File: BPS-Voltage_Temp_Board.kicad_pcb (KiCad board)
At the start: 2 copper layers, 85.8 x 48.6 mm, 61 parts, among them J2 voltage taps, J3 temptap0, J4 I-CanConn, J5 I-CanConn, J7 temptap1, J8 extratemp1, J9 extratemp2, Q1 mmftp3334k, SW1 BMS_BOOT, U1 ADS131M08QPBSRQ1, U2 BQ7692003PW, U3 PeripheralSOM, U4 ISO1641BDR, U5 EL3H7, U6 EL3H7

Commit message: Addressed some concerns
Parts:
- moved J2 1.84 mm to (177.5, 54.4)
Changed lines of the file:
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@@
 	(footprint "Connector_Molex:Molex_Nano-Fit_105314-xx10_2x05_P2.50mm_Horizontal"
 		(layer "F.Cu")
-		(at 176.32 53)
+		(at 177.52 54.4)
 		(descr "Molex Nano-Fit Power Connectors, 105314-xx10, 5 Pins per row (http://www.molex.com/pdm_docs/sd/1053141208_sd.pdf), generated with kicad-footprint-generator")
 		(tags "connector Molex Nano-Fit top entry")

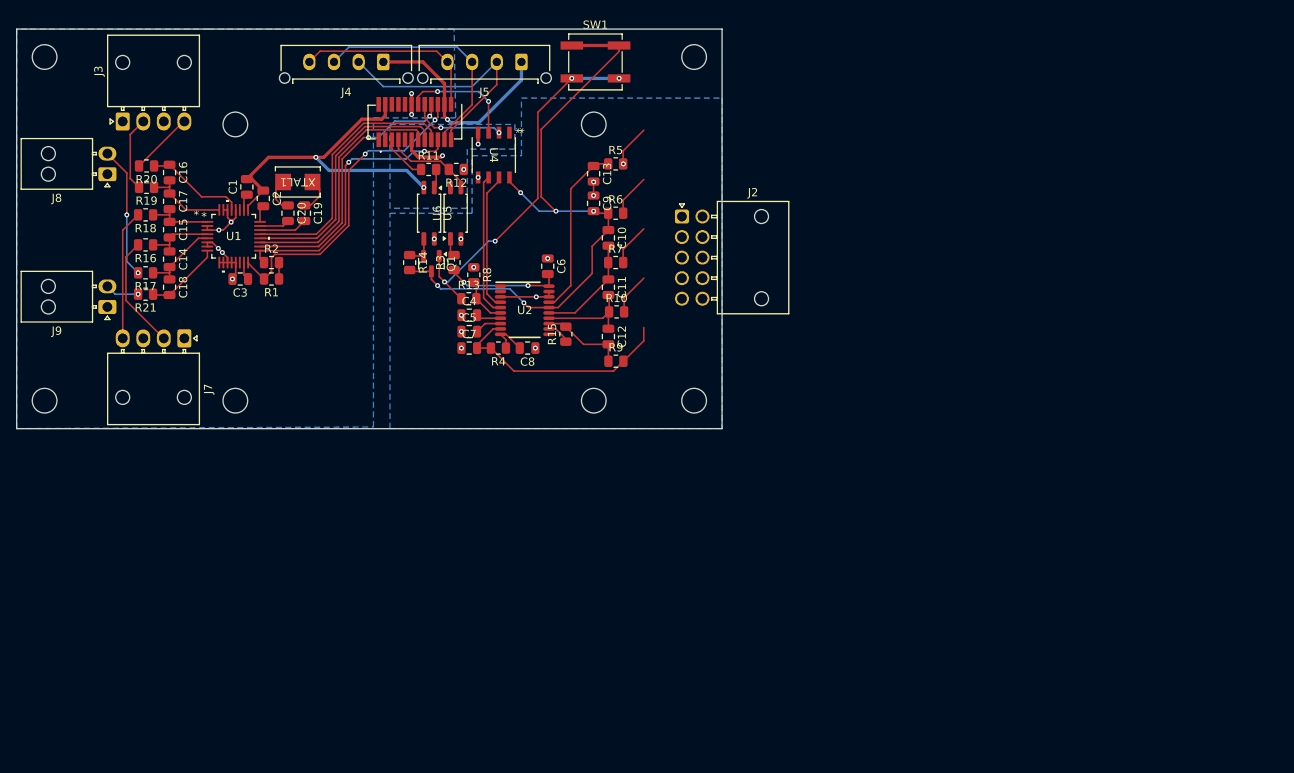
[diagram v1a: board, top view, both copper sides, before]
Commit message: schematic should be finished. Preliminary layout with changes from review
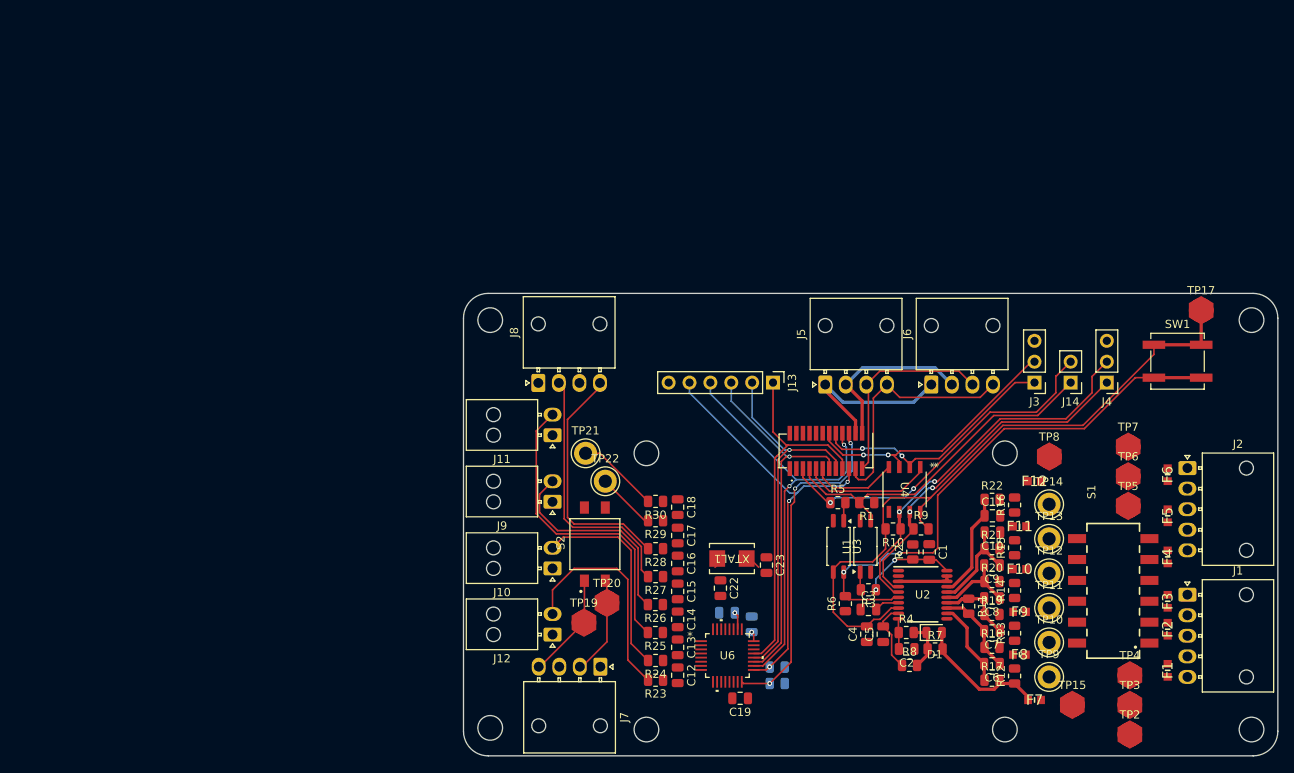
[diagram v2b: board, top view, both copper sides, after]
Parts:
- removed the H1 at (100.0, 76.8)
- removed the H1 at (179.0, 76.8)
- removed the H1 at (179.0, 35.0)
- removed the H1 at (100.0, 35.0)
- removed Q1: mmftp3334k, Package_TO_SOT_SMD:SOT-23
- added C21: 220nF, Capacitor_SMD:C_0805_2012Metric, B.Cu at (186.0, 104.0)
- added C22: 36pF, Capacitor_SMD:C_0805_2012Metric, F.Cu at (182.2, 99.6)
- added C23: 36pF, Capacitor_SMD:C_0805_2012Metric, F.Cu at (187.8, 96.8)
- added D1: D_Zener_Small, Diode_SMD:D_0805_2012Metric, F.Cu at (208.2, 105.0)
- added F1: 10mA, UTSVT_Special:ptc_fuse_FUSC1607X75N, F.Cu at (236.6, 109.6)
- added F10: 10mA, UTSVT_Special:ptc_fuse_FUSC1607X75N, F.Cu at (218.6, 97.3)
- added F11: 10mA, UTSVT_Special:ptc_fuse_FUSC1607X75N, F.Cu at (218.6, 92.1)
- added F12: 40mA, UTSVT_Special:ptc_fuse_FUSC1607X75N, F.Cu at (220.4, 86.6)
- added F2: 10mA, UTSVT_Special:ptc_fuse_FUSC1607X75N, F.Cu at (236.6, 104.6)
- added F3: 10mA, UTSVT_Special:ptc_fuse_FUSC1607X75N, F.Cu at (236.6, 101.2)
- added F4: 10mA, UTSVT_Special:ptc_fuse_FUSC1607X75N, F.Cu at (236.6, 95.8)
- added F5: 10mA, UTSVT_Special:ptc_fuse_FUSC1607X75N, F.Cu at (236.6, 90.8)
- added F6: 40mA, UTSVT_Special:ptc_fuse_FUSC1607X75N, F.Cu at (236.6, 85.8)
- added F7: 10mA, UTSVT_Special:ptc_fuse_FUSC1607X75N, F.Cu at (220.4, 113.2)
- added F8: 10mA, UTSVT_Special:ptc_fuse_FUSC1607X75N, F.Cu at (218.6, 107.7)
- added F9: 10mA, UTSVT_Special:ptc_fuse_FUSC1607X75N, F.Cu at (218.6, 102.5)
- added H1: MountingHole, MountingHole:MountingHole_3mm, F.Cu at (154.2, 67.0)
- added H1: MountingHole, MountingHole:MountingHole_3mm, F.Cu at (246.8, 116.8)
- added H1: MountingHole, MountingHole:MountingHole_3mm, F.Cu at (154.2, 116.6)
- added H1: MountingHole, MountingHole:MountingHole_3mm, F.Cu at (246.8, 67.0)
- added J1: VoltTap2, Connector_Molex:Molex_Nano-Fit_105313-xx05_1x05_P2.50mm_Horizontal, F.Cu at (239.0, 100.4)
- added J10: extratemp3, Connector_Molex:Molex_Nano-Fit_105313-xx02_1x02_P2.50mm_Horizontal, F.Cu at (161.8, 97.2)
- added J11: extratemp2, Connector_Molex:Molex_Nano-Fit_105313-xx02_1x02_P2.50mm_Horizontal, F.Cu at (161.8, 81.0)
- added J12: extratemp4, Connector_Molex:Molex_Nano-Fit_105313-xx02_1x02_P2.50mm_Horizontal, F.Cu at (161.8, 105.2)
- added J13: SPI test, Connector_PinHeader_2.54mm:PinHeader_1x06_P2.54mm_Vertical, F.Cu at (188.6, 74.6)
- added J14: alert/en_test, Connector_PinHeader_2.54mm:PinHeader_1x02_P2.54mm_Vertical, F.Cu at (224.8, 74.6)
- added J6: I-CAN connector, Connector_Molex:Molex_Nano-Fit_105313-xx04_1x04_P2.50mm_Horizontal, F.Cu at (207.8, 74.8)
- added R22: 100Ω, Resistor_SMD:R_0805_2012Metric, F.Cu at (215.2, 88.8)
- added R23: 50Ω, Resistor_SMD:R_0805_2012Metric, F.Cu at (174.3, 110.8)
- added R24: 50Ω, Resistor_SMD:R_0805_2012Metric, F.Cu at (174.3, 108.4)
- added R25: 50Ω, Resistor_SMD:R_0805_2012Metric, F.Cu at (174.3, 105.0)
- added R26: 50Ω, Resistor_SMD:R_0805_2012Metric, F.Cu at (174.3, 101.6)
- added R27: 50Ω, Resistor_SMD:R_0805_2012Metric, F.Cu at (174.3, 98.2)
- added R28: 50Ω, Resistor_SMD:R_0805_2012Metric, F.Cu at (174.3, 94.8)
- added R29: 50Ω, Resistor_SMD:R_0805_2012Metric, F.Cu at (174.3, 91.4)
- added R30: 50Ω, Resistor_SMD:R_0805_2012Metric, F.Cu at (174.3, 89.0)
- added R31: 100kΩ, Resistor_SMD:R_0805_2012Metric, B.Cu at (189.1, 111.2)
- added R32: 100kΩ, Resistor_SMD:R_0805_2012Metric, B.Cu at (189.1, 109.2)
- added S1: 418121270806, footprints:418121270806, F.Cu at (230.0, 99.9)
- added S2: DS04-254-2-02BK-SMT-TR, footprints:SW_DS04-254-2-02BK-SMT-TR, F.Cu at (166.9, 94.2)
- added TP10: 4&5inject, TestPoint:TestPoint_Keystone_5010-5014_Multipurpose, F.Cu at (222.2, 106.2)
- added TP11: 3&4inject, TestPoint:TestPoint_Keystone_5010-5014_Multipurpose, F.Cu at (222.2, 102.0)
- added TP12: 2&3inject, TestPoint:TestPoint_Keystone_5010-5014_Multipurpose, F.Cu at (222.2, 97.8)
- added TP13: 1&2inject, TestPoint:TestPoint_Keystone_5010-5014_Multipurpose, F.Cu at (222.2, 93.6)
- added TP14: cellgndinject, TestPoint:TestPoint_Keystone_5010-5014_Multipurpose, F.Cu at (222.2, 89.4)
- added TP15: BAT tap, UTSVT_Special:TestPoint_HEX_3mmID, F.Cu at (225.0, 113.8)
- added TP17: regout testpoint, UTSVT_Special:TestPoint_HEX_3mmID, F.Cu at (240.7, 65.8)
- added TP19: t0test, UTSVT_Special:TestPoint_HEX_3mmID, F.Cu at (165.6, 103.8)
- added TP2: last_cell, UTSVT_Special:TestPoint_HEX_3mmID, F.Cu at (232.0, 117.4)
- added TP20: t1test, UTSVT_Special:TestPoint_HEX_3mmID, F.Cu at (168.4, 101.4)
- added TP21: temp0inject, TestPoint:TestPoint_Keystone_5010-5014_Multipurpose, F.Cu at (165.8, 83.2)
- added TP22: temp1inject, TestPoint:TestPoint_Keystone_5010-5014_Multipurpose, F.Cu at (168.2, 86.6)
- added TP3: 4&5 COM, UTSVT_Special:TestPoint_HEX_3mmID, F.Cu at (232.0, 113.8)
- added TP4: 3&4 COM, UTSVT_Special:TestPoint_HEX_3mmID, F.Cu at (232.0, 110.2)
- added TP5: 2&3 COM, UTSVT_Special:TestPoint_HEX_3mmID, F.Cu at (231.8, 89.6)
- added TP6: 1&2 COM, UTSVT_Special:TestPoint_HEX_3mmID, F.Cu at (231.8, 86.0)
- added TP7: GND2, UTSVT_Special:TestPoint_HEX_3mmID, F.Cu at (231.8, 82.4)
- added TP8: VSS tap, UTSVT_Special:TestPoint_HEX_3mmID, F.Cu at (222.2, 83.6)
- added TP9: last_inject, TestPoint:TestPoint_Keystone_5010-5014_Multipurpose, F.Cu at (222.2, 110.4)
- C1: value 1μF -> 4.7pF
- C12, C13: value 1μF -> 4.7nF
- C19: value 36pF -> 1μF
- C2: value 220nF -> 10μF
- C20: value 36pF -> 1μF; moved to B.Cu
- C4: value 1μF -> 4.7μF
- C5: value 4.7μF -> 1μF
- C6: value 4.7pF -> 1μF
- C8: value 10μF -> 1μF
- J2: value voltage taps -> VoltTap1; footprint Connector_Molex:Molex_Nano-Fit_105314-xx10_2x05_P2.50mm_Horizontal -> Connector_Molex:Molex_Nano-Fit_105313-xx05_1x05_P2.50mm_Horizontal
- J3: value temptap0 -> psom bms i2c test; footprint Connector_Molex:Molex_Nano-Fit_105313-xx04_1x04_P2.50mm_Horizontal -> Connector_PinHeader_2.54mm:PinHeader_1x03_P2.54mm_Vertical
- J4: value I-CanConn -> bms i2c test; footprint Connector_Molex:Molex_Micro-Fit_3.0_43650-0415_1x04_P3.00mm_Vertical -> Connector_PinHeader_2.54mm:PinHeader_1x03_P2.54mm_Vertical
- J5: value I-CanConn -> I-CAN connector; footprint Connector_Molex:Molex_Micro-Fit_3.0_43650-0415_1x04_P3.00mm_Vertical -> Connector_Molex:Molex_Nano-Fit_105313-xx04_1x04_P2.50mm_Horizontal
- J7: value temptap1 -> temptap0
- J8: value extratemp1 -> temptap1; footprint Connector_Molex:Molex_Nano-Fit_105313-xx02_1x02_P2.50mm_Horizontal -> Connector_Molex:Molex_Nano-Fit_105313-xx04_1x04_P2.50mm_Horizontal
- J9: value extratemp2 -> extratemp1
- R1: value 100kΩ -> 10kΩ
- R10, R6, R9: value 100Ω -> 10kΩ
- R11: value 2kΩ -> 0Ω
- R12, R13: value 10kΩ -> 0Ω
- R14: value 100kΩ -> 0Ω
- R16: value 50Ω -> 0Ω
- R17, R18, R19, R20, R21: value 50Ω -> 100Ω
- R2: value 100kΩ -> 500kΩ
- R3: value 500kΩ -> 100Ω
- R5: value 100Ω -> 2kΩ
- R7: value 100Ω -> 1kΩ
- R8: value 10kΩ -> 1kΩ
- U1: value ADS131M08QPBSRQ1 -> EL3H7; footprint footprints:TQFP32_PBS_TEX -> Package_SO:SSOP-4_4.4x2.6mm_P1.27mm
- U3: value PeripheralSOM -> EL3H7; footprint UTSVT_Special:PeripheralSOM -> Package_SO:SSOP-4_4.4x2.6mm_P1.27mm
- U5: value EL3H7 -> PeripheralSOM; footprint Package_SO:SSOP-4_4.4x2.6mm_P1.27mm -> UTSVT_Special:PeripheralSOM
- U6: value EL3H7 -> ADS131M08QPBSRQ1; footprint Package_SO:SSOP-4_4.4x2.6mm_P1.27mm -> footprints:TQFP32_PBS_TEX
- moved R18 115.6 mm to (215.2, 106.8), turned to 0 degrees
- moved J3 115.4 mm to (220.4, 74.6), turned to 180 degrees
- moved R19 115.2 mm to (215.2, 102.8), turned to 0 degrees
- moved R20 114.6 mm to (215.2, 98.8), turned to 0 degrees
- moved R17 114.2 mm to (215.2, 110.8), turned to 0 degrees
- moved R16 110.3 mm to (218.0, 89.5), turned to 90 degrees
- moved R21 107.5 mm to (215.2, 94.8), turned to 0 degrees
- moved J4 96.3 mm to (229.2, 74.6)
- moved C2 95.5 mm to (204.8, 107.0), turned to 180 degrees
- moved C1 94.1 mm to (207.6, 95.2), turned to -90 degrees
- moved R12 91.7 mm to (218.0, 110.3), turned to 90 degrees
- moved C3 86.3 mm to (200.2, 102.2), turned to 0 degrees
- moved U1 85.6 mm to (199.8, 94.5), turned to 90 degrees
- moved R2 85.6 mm to (205.6, 95.2), turned to 90 degrees
- moved R11 84.5 mm to (212.4, 101.8), turned to -90 degrees
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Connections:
- C1 pad 1: +3.3V -> GND2
- C1 pad 2: GND -> Net-(U2-ALERT)
- C10 pad 1: /VC1 -> GND2
- C10 pad 2: /VC2 -> /VC1
- C11 pad 1: /VC2 -> /VC0
- C11 pad 2: /VC3 -> GND2
- C12 pad 1: /VC3 -> /Thermistor town/AIN6
- C12 pad 2: /VC4 -> /Thermistor town/AIN7
- C13 pad 1: /VC0 -> /Thermistor town/AIN5
- C13 pad 2: GND2 -> /Thermistor town/AIN6
- C14 pad 1: /Thermistor town/AIN3 -> /Thermistor town/AIN4
- C14 pad 2: /Thermistor town/AIN4 -> /Thermistor town/AIN5
- C15 pad 1: /Thermistor town/AIN2 -> /Thermistor town/AIN3
- C15 pad 2: /Thermistor town/AIN3 -> /Thermistor town/AIN4
- C16 pad 1: /Thermistor town/AIN0 -> /Thermistor town/AIN2
- C16 pad 2: /Thermistor town/AIN1 -> /Thermistor town/AIN3
- C18 pad 1: /Thermistor town/AIN4 -> /Thermistor town/AIN0
- C18 pad 2: /Thermistor town/AIN5 -> /Thermistor town/AIN1
- C19 pad 1: Net-(C19-Pad1) -> +3.3VA
- C19 pad 2: /Thermistor town/xtal2 -> GNDA
- C2 pad 1: GND -> GND2
- C2 pad 2: Net-(U1-CAP) -> Net-(U2-BAT)
- C20 pad 1: Net-(C20-Pad1) -> +3.3V
- C20 pad 2: /Thermistor town/xtal1 -> GND
- C3 pad 1: +3.3VA -> GND2
- C3 pad 2: GNDA -> Net-(U2-CAP1)
- C4 pad 2: Net-(U2-CAP1) -> /regout
- C5 pad 2: Net-(U2-REGOUT) -> Net-(U2-REGSRC)
- C6 pad 1: GND2 -> /VC4
- C6 pad 2: Net-(U2-ALERT) -> /VC5
- C7 pad 1: GND2 -> /VC3
- C7 pad 2: /cell4+ -> /VC4
- C8 pad 1: GND2 -> /VC2
- C8 pad 2: Net-(U2-BAT) -> /VC3
- C9 pad 1: GND2 -> /VC1
- C9 pad 2: /VC1 -> /VC2
- J2 pad 1: GND2 -> Net-(J2-Pin_1)
- J2 pad 3: /1&2COM -> Net-(J2-Pin_3)
- J2 pad 5: /2&3COM -> Net-(J2-Pin_5)
- J3 pad 1: GNDA -> /psSDA
- J3 pad 2: /Thermistor town/temp1 -> /psSCL
- J3 pad 3: GNDA -> GND
- J4 pad 1: +12V -> /bmSDA
- J4 pad 2: /I-CAN_H -> /bmSCL
- J4 pad 3: /I-CAN_L -> GND2
- J5 pad 2: /I-CAN_H -> GNDPWR
- J5 pad 3: /I-CAN_L -> /I-CAN_H
- J5 pad 4: GNDPWR -> /I-CAN_L
- J7 pad 2: /Thermistor town/temp3 -> Net-(J7-Pin_2)
- J7 pad 4: /Thermistor town/temp2 -> Net-(J7-Pin_4)
- J8 pad 2: /Thermistor town/temp4 -> /Thermistor town/temp3
- J9 pad 2: /Thermistor town/temp5 -> /Thermistor town/temp4
- R1 pad 1: +3.3V -> GND
- R1 pad 2: /SYNC -> /bmsALERT
- R10 pad 1: /VC3 -> /bmSCL
- R10 pad 2: /3&4COM -> /regout
- R11 pad 1: /bmsEN -> /VC3
- R11 pad 2: Net-(R11-Pad2) -> /VC4
- R12 pad 1: GND -> /last_cell
- R12 pad 2: /bmsALERT -> /4&5COM
- R13 pad 1: Net-(Q1-D) -> /4&5COM
- R13 pad 2: Net-(U2-TS1) -> /3&4COM
- R14 pad 1: Net-(Q1-G) -> /3&4COM
- R14 pad 2: /VC1 -> /2&3COM
- R15 pad 1: /VC5 -> /2&3COM
- R15 pad 2: /VC4 -> /1&2COM
- R16 pad 1: /Thermistor town/AIN3 -> /1&2COM
- R16 pad 2: /Thermistor town/temp3 -> GND2
- R17 pad 1: /Thermistor town/AIN4 -> /VC5
- R17 pad 2: /Thermistor town/temp4 -> /last_cell
- R18 pad 1: /Thermistor town/AIN2 -> /VC4
- R18 pad 2: /Thermistor town/temp2 -> /4&5COM
- R19 pad 1: /Thermistor town/AIN1 -> /VC3
- R19 pad 2: /Thermistor town/temp1 -> /3&4COM
- R2 pad 1: /adCS -> Net-(U2-ALERT)
- R2 pad 2: +3.3V -> GND2
- R20 pad 1: /Thermistor town/AIN0 -> /VC2
- R20 pad 2: /Thermistor town/temp0 -> /2&3COM
- R21 pad 1: /Thermistor town/AIN5 -> /VC1
- R21 pad 2: /Thermistor town/temp5 -> /1&2COM
- R4 pad 2: /cell4+ -> Net-(D1-K)
- R5 pad 1: /VC0 -> /bmsEN
- R5 pad 2: GND2 -> Net-(R5-Pad2)
- R6 pad 1: /VC1 -> GND2
- R6 pad 2: /1&2COM -> /BMSboot
- R7 pad 1: /VC2 -> Net-(D1-K)
- R7 pad 2: /2&3COM -> /last_cell
- R8 pad 1: GND2 -> Net-(U2-REGSRC)
- R8 pad 2: Net-(U2-TS1) -> Net-(D1-K)
- R9 pad 1: /VC4 -> /bmSDA
- R9 pad 2: /cell4+ -> /regout
- SW1 pad 1: /VC1 -> /regout
- SW1 pad 2: Net-(Q1-D) -> /BMSboot
- U1 pad 1: /Thermistor town/AIN2 -> Net-(R3-Pad2)
- U1 pad 2: GNDA -> GND2
- U1 pad 3: GNDA -> /bmsALERT
- U1 pad 4: /Thermistor town/AIN3 -> +3.3V
- U2 pad 6: Net-(U2-TS1) -> /BMSboot
- U2 pad 8: Net-(U2-REGOUT) -> /regout
- U2 pad 9: /cell4+ -> Net-(U2-REGSRC)
- U3 pad 1: unconnected-(U3-SPI2_MOSI-Pad1) -> Net-(R5-Pad2)
- U3 pad 2: +3.3V -> GND
- U3 pad 3: unconnected-(U3-SPI2_MISO-Pad3) -> /regout
- U3 pad 4: GND -> /BMSboot
- U4 pad 8: /VC1 -> /regout
- U5 pad 1: Net-(R11-Pad2) -> unconnected-(U5-SPI2_MOSI-Pad1)
- U5 pad 2: GND -> +3.3V
- U5 pad 3: Net-(Q1-G) -> unconnected-(U5-SPI2_MISO-Pad3)
- U5 pad 4: GND2 -> GND
- U6 pad 1: Net-(R3-Pad2) -> /Thermistor town/AIN2
- U6 pad 2: GND2 -> GNDA
- U6 pad 3: /bmsALERT -> GNDA
- U6 pad 4: +3.3V -> /Thermistor town/AIN3
- XTAL1 pad 1: Net-(C19-Pad1) -> Net-(C23-Pad1)
- XTAL1 pad 2: Net-(C20-Pad1) -> Net-(C22-Pad1)
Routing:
- net /regout: track 0.00 -> 84.0 mm
- net /BMSboot: track 0.00 -> 67.1 mm, vias 0 -> 2
- net /VC1: track 79.2 -> 12.8 mm, vias 5 -> 0
- net Net-(Q1-D): track 43.9 -> 0.00 mm, vias 4 -> 0
- net GND: track 48.8 -> 10.7 mm, vias 5 -> 0
- net /bmsEN: track 5.70 -> 43.2 mm, vias 0 -> 2
- net /Thermistor town/temp5: track 4.16 -> 37.4 mm, vias 1 -> 0
- net /bmsALERT: track 11.1 -> 42.9 mm
- net /bmSCL: track 17.5 -> 46.1 mm, vias 0 -> 2
- net /cell4+: track 28.6 -> 0.00 mm
- net /Thermistor town/temp7: track 0.00 -> 27.0 mm
- net /bmSDA: track 16.8 -> 43.4 mm, vias 0 -> 2
- net /Thermistor town/temp6: track 0.00 -> 25.0 mm
- net /psSDA: track 11.4 -> 31.4 mm
- net /DRDY: track 33.3 -> 53.0 mm
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- removed copper zone on B.Cu, net GND
- removed copper zone on B.Cu, net GND2
- removed copper zone on B.Cu, net GNDA
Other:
- board size 85.8 x 48.6 mm -> 99.1 x 56.2 mm

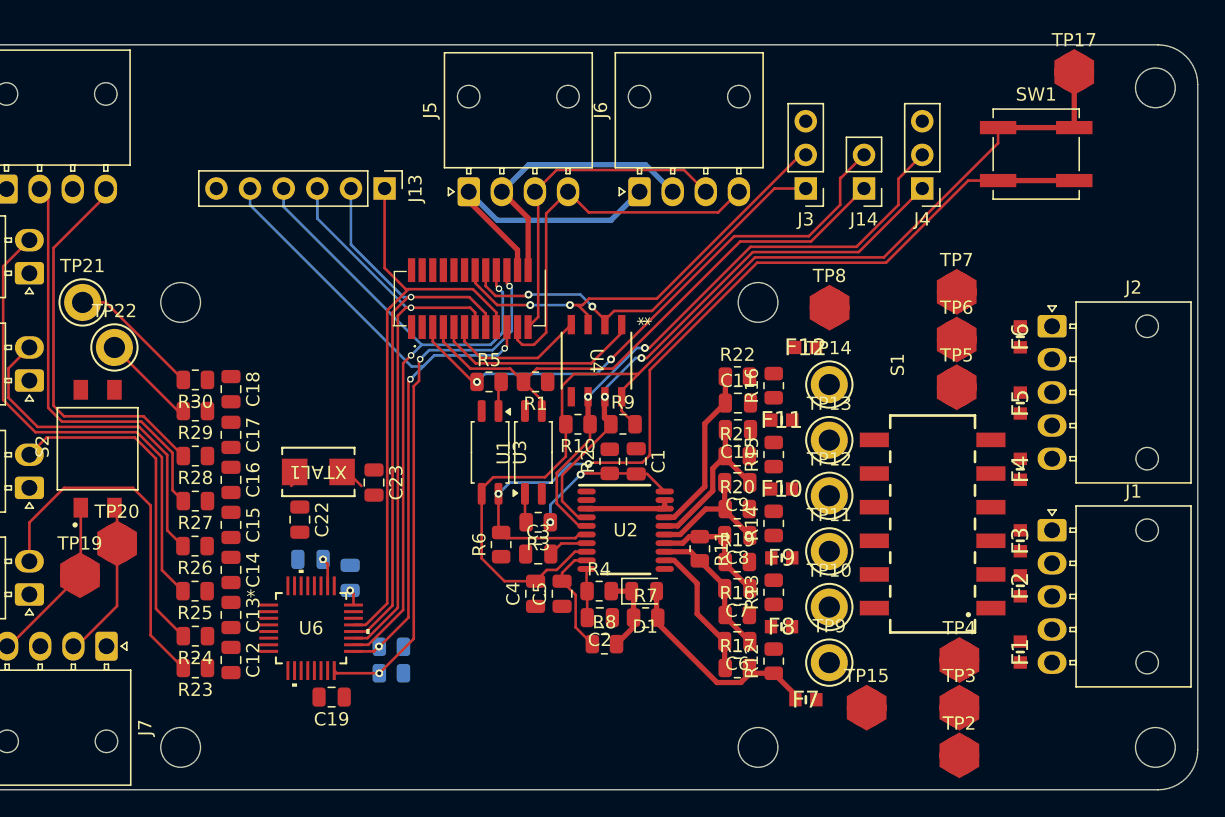
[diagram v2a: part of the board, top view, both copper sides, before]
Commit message: most traces ok, need to add pwr for adc & gnd everywhere
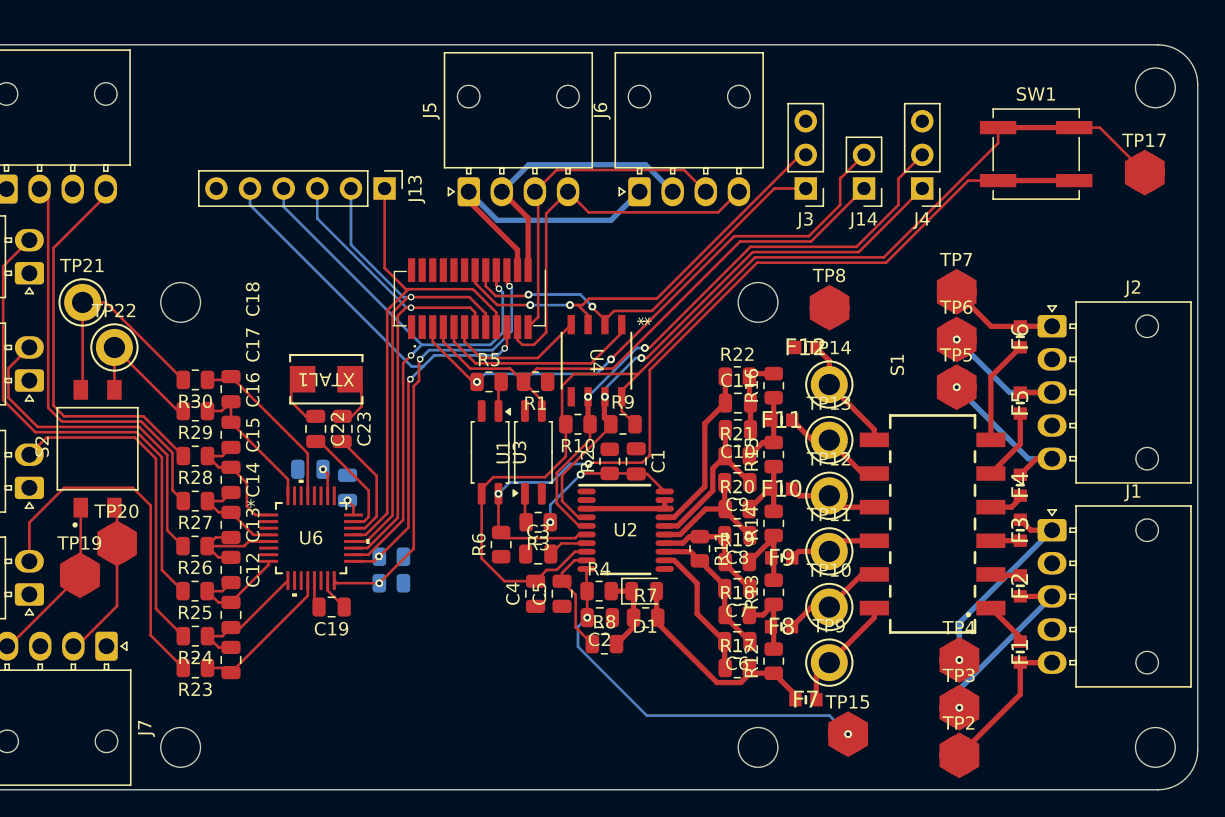
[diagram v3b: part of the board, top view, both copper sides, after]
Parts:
- moved TP17 9.28 mm to (246.0, 73.4)
- moved XTAL1 7.03 mm to (184.2, 89.0)
- moved C22 6.95 mm to (183.4, 92.8)
- moved C21 6.80 mm to (185.8, 97.2)
- moved C19 6.80 mm to (184.6, 106.2)
- moved C20 6.80 mm to (183.0, 95.8)
- moved R31 6.80 mm to (189.1, 104.4)
- moved R32 6.80 mm to (189.1, 102.4)
- moved U6 6.80 mm to (183.1, 101.0)
- moved C23 4.71 mm to (185.4, 92.8)
- moved TP15 2.44 mm to (223.6, 115.8)
- moved F4 1.20 mm to (236.6, 97.0)
- moved F3 0.80 mm to (236.6, 100.4)
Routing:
- net Net-(U2-BAT): track 3.70 -> 29.3 mm, vias 0 -> 2
- net Net-(J1-Pin_1): track 0.00 -> 15.4 mm, vias 0 -> 1
- net Net-(J1-Pin_3): track 0.00 -> 13.7 mm, vias 0 -> 1
- net /Thermistor town/AIN0: track 0.00 -> 13.3 mm
- net Net-(J2-Pin_5): track 0.00 -> 12.3 mm, vias 0 -> 1
- net Net-(J1-Pin_5): track 0.00 -> 11.3 mm
- net /Thermistor town/AIN7: track 0.00 -> 11.3 mm
- net Net-(J2-Pin_3): track 0.00 -> 11.3 mm, vias 0 -> 1
- net /Thermistor town/AIN1: track 0.00 -> 10.9 mm
- net /Thermistor town/AIN6: track 0.00 -> 9.94 mm
- net /Thermistor town/AIN2: track 0.00 -> 9.54 mm
- net /Thermistor town/AIN4: track 0.00 -> 9.02 mm
- net /Thermistor town/xtal2: track 0.00 -> 8.85 mm
- net /Thermistor town/xtal1: track 0.00 -> 8.82 mm
- net Net-(F12-Pad1): track 0.00 -> 8.80 mm
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
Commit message: Preliminary schematic done. need to adjust silkscreen and what not
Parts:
- C20, C21, R31, R32: moved to F.Cu
- C22, C23: value 36pF -> 18pF
- moved XTAL1 12.7 mm to (190.6, 100.0), turned to 90 degrees
- moved C23 12.5 mm to (190.4, 104.2), turned to 180 degrees
- moved C22 7.68 mm to (190.4, 95.8), turned to 180 degrees
- moved R31 5.84 mm to (184.6, 108.1), turned to 90 degrees
- moved R32 4.89 mm to (186.6, 106.6), turned to -90 degrees
- moved TP8 3.41 mm to (225.6, 83.8)
- moved C19 2.79 mm to (182.6, 108.2), turned to -90 degrees
- moved C5 2.25 mm to (200.7, 107.0), turned to 0 degrees
- moved TP2 2.24 mm to (230.0, 116.4)
- moved TP7 2.06 mm to (230.0, 83.4)
- moved TP4 2.01 mm to (230.0, 110.4)
- moved TP5 1.81 mm to (230.0, 89.4)
- moved C21 0.94 mm to (186.3, 96.4)
- moved C4 0.68 mm to (200.7, 105.0), turned to 0 degrees
- moved TP3 0.45 mm to (231.8, 113.4)
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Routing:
- net +3.3V: track 18.2 -> 69.4 mm, vias 1 -> 5
- net +3.3VA: track 2.52 -> 42.5 mm, vias 0 -> 2
- net GNDA: track 2.14 -> 40.4 mm, vias 0 -> 11
- net /DRDY: track 46.2 -> 63.0 mm
- net /adMOSI: track 37.7 -> 53.7 mm, vias 0 -> 1
- net /adSCLK: track 39.0 -> 53.4 mm
- net /adMISO: track 38.6 -> 52.8 mm
- net /adCS: track 45.7 -> 58.5 mm, vias 3 -> 2
- net /SYNC: track 34.2 -> 45.5 mm, vias 3 -> 2
- net GND2: track 12.6 -> 17.0 mm, vias 0 -> 15
- net GND: track 10.7 -> 7.32 mm, vias 0 -> 7
- net /bmsALERT: track 42.9 -> 46.3 mm
- net /Thermistor town/xtal1: track 8.82 -> 5.88 mm
- net /Thermistor town/xtal2: track 8.85 -> 6.23 mm
- net Net-(J1-Pin_5): track 11.3 -> 13.9 mm
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- added copper zone on B.Cu, net GND
- added copper zone on B.Cu, net GND2
- added copper zone on B.Cu, net GNDA
